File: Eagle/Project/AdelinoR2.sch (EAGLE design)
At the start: 79 parts, among them J1 DC-044-A, J2 YELLOW-8P-2.54, J3 YELLOW-6P-2.54, J4 YELLOW-8P-2.54, J5 YELLOW-8P-2.54, J6 4P-2.0, J7 YELLOW-2X3P-2.54, J8 4P-2.0, Q1 NCE3407A, Q2 CJ2305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

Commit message: Routing wip.
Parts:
- removed D1, D2: 1K 1/10W, Seeed-Fuse:SMD-ESD-CG0603MLC-05E
- added ESD1: PRTR5V0U2X, Seeed-OPL-2017-01-Diode-james:SMD-DIODE-TVS-5.5V
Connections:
- net GND: no longer D1.1, D2.1
- net N$1: now also ESD1.IO2; no longer D1.2
- net N$2: now also ESD1.IO1; no longer D2.2
- net N$9: now also ESD1.VCC
- net UGND: now also ESD1.GND
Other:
- moved on the sheet: F1, L1, R2, R3, USB1

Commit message: Add ATECC608 crypto chip; routing wip.
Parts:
- added U6: ATECC608-SOIC8, Adelino-Misc:ATECC608(SOIC8)
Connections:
- removed net PIN_D2: J5.3, J6.2, U3.GPIO4, U4.PD1(SDA/INT1), U5.PD1(SDA/INT1)
- removed net PIN_D3: J5.4, J6.1, U3.GPIO5, U4.PD0(OC0B/SCL/INT0), U5.PD0(OC0B/SCL/INT0)
- removed net _ESP: D8.+, R28.2
- new net N$4: D8.-, R28.1
- new net PIN_D2_SDA: J5.3, J6.2, U3.GPIO4, U4.PD1(SDA/INT1), U5.PD1(SDA/INT1), U6.SDA
- new net PIN_D3_SCL: J5.4, J6.1, U3.GPIO5, U4.PD0(OC0B/SCL/INT0), U5.PD0(OC0B/SCL/INT0), U6.SCL
- net +3V3: now also D8.+; no longer R28.1
- net +5V: now also U6.VCC
- net GND: now also U6.GND
- net GPIO2_LED: now also R28.2; no longer D8.-
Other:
- note added: "Security"
- moved on the sheet: D4, D5, D6, D7, D8, R13, R14, R15, R16, R17, R18, R19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

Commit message: Routing wip.
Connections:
- net +3V3: now also R28.1; no longer D8.+
- net GPIO2_LED: now also D8.-; no longer R28.2
- net N$4: now also D8.+, R28.2; no longer D8.-, R28.1
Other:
- note added: "ICSP"
- moved on the sheet: D8, R28
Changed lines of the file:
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@@
 <setting verticaltext="up"/>
 </settings>
-<grid distance="0.05" unitdist="inch" unit="inch" style="lines" multiple="1" display="no" altdistance="0.01" altunitdist="inch" altunit="inch"/>
+<grid distance="0.1" unitdist="inch" unit="inch" style="lines" multiple="1" display="no" altdistance="0.01" altunitdist="inch" altunit="inch"/>
 <layers>
 <layer number="1" name="Top" color="4" fill="1" visible="no" active="no"/>
@@
 <text x="-66.04" y="-85.09" size="2.54" layer="97">Grove Serial</text>
 <text x="13.97" y="-125.73" size="6.4516" layer="97">Security</text>
+<text x="-79.248" y="-130.556" size="2.54" layer="97">ICSP</text>
 </plain>
 <instances>
@@
 <attribute name="VALUE" x="71.628" y="-54.356" size="1.27" layer="96" ratio="10"/>
 </instance>
-<instance part="D8" gate="G$1" x="191.77" y="-101.6" smashed="yes">
-<attribute name="NAME" x="189.992" y="-99.822" size="1.27" layer="95" ratio="10" rot="R180"/>
-<attribute name="VALUE" x="193.548" y="-103.124" size="1.016" layer="96" ratio="10"/>
-<attribute name="LABEL" x="193.548" y="-101.092" size="1.4224" layer="96"/>
+<instance part="D8" gate="G$1" x="201.93" y="-101.6" smashed="yes">
+<attribute name="NAME" x="200.152" y="-99.822" size="1.27" layer="95" ratio="10" rot="R180"/>
+<attribute name="VALUE" x="203.708" y="-103.124" size="1.016" layer="96" ratio="10"/>
+<attribute name="LABEL" x="203.708" y="-101.092" size="1.4224" layer="96"/>
 </instance>
 <instance part="+3V34" gate="G$1" x="182.88" y="-93.726" smashed="yes">
@@
 <attribute name="VALUE" x="71.628" y="-92.456" size="1.27" layer="96" ratio="10"/>
 </instance>
-<instance part="R28" gate="G$1" x="201.93" y="-101.6" smashed="yes">
-<attribute name="NAME" x="203.708" y="-101.092" size="1.27" layer="95" ratio="10"/>
-<attribute name="VALUE" x="203.708" y="-103.378" size="1.27" layer="96" ratio="10"/>
+<instance part="R28" gate="G$1" x="191.77" y="-101.6" smashed="yes">
+<attribute name="NAME" x="193.548" y="-101.092" size="1.27" layer="95" ratio="10"/>
+<attribute name="VALUE" x="193.548" y="-103.378" size="1.27" layer="96" ratio="10"/>
 </instance>
 <instance part="R29" gate="G$1" x="191.77" y="-109.22" smashed="yes">
@@
 <wire x1="187.96" y1="-109.22" x2="182.88" y2="-109.22" width="0.1524" layer="91"/>
 <wire x1="182.88" y1="-109.22" x2="182.88" y2="-101.6" width="0.1524" layer="91"/>
-<pinref part="D8" gate="G$1" pin="+"/>
+<pinref part="R28" gate="G$1" pin="1"/>
 <wire x1="182.88" y1="-101.6" x2="182.88" y2="-96.266" width="0.1524" layer="91"/>
 <wire x1="187.96" y1="-101.6" x2="182.88" y2="-101.6" width="0.1524" layer="91"/>
@@
 <junction x="212.09" y="-109.22"/>
 <label x="226.06" y="-109.22" size="1.4224" layer="95" rot="R180"/>
-<pinref part="R28" gate="G$1" pin="2"/>
+<pinref part="D8" gate="G$1" pin="-"/>
 <wire x1="205.74" y1="-101.6" x2="212.09" y2="-101.6" width="0.1524" layer="91"/>
 </segment>
@@
 <net name="N$4" class="0">
 <segment>
-<pinref part="R28" gate="G$1" pin="1"/>
-<pinref part="D8" gate="G$1" pin="-"/>
+<pinref part="D8" gate="G$1" pin="+"/>
+<pinref part="R28" gate="G$1" pin="2"/>
 <wire x1="198.12" y1="-101.6" x2="195.58" y2="-101.6" width="0.1524" layer="91"/>
 </segment>

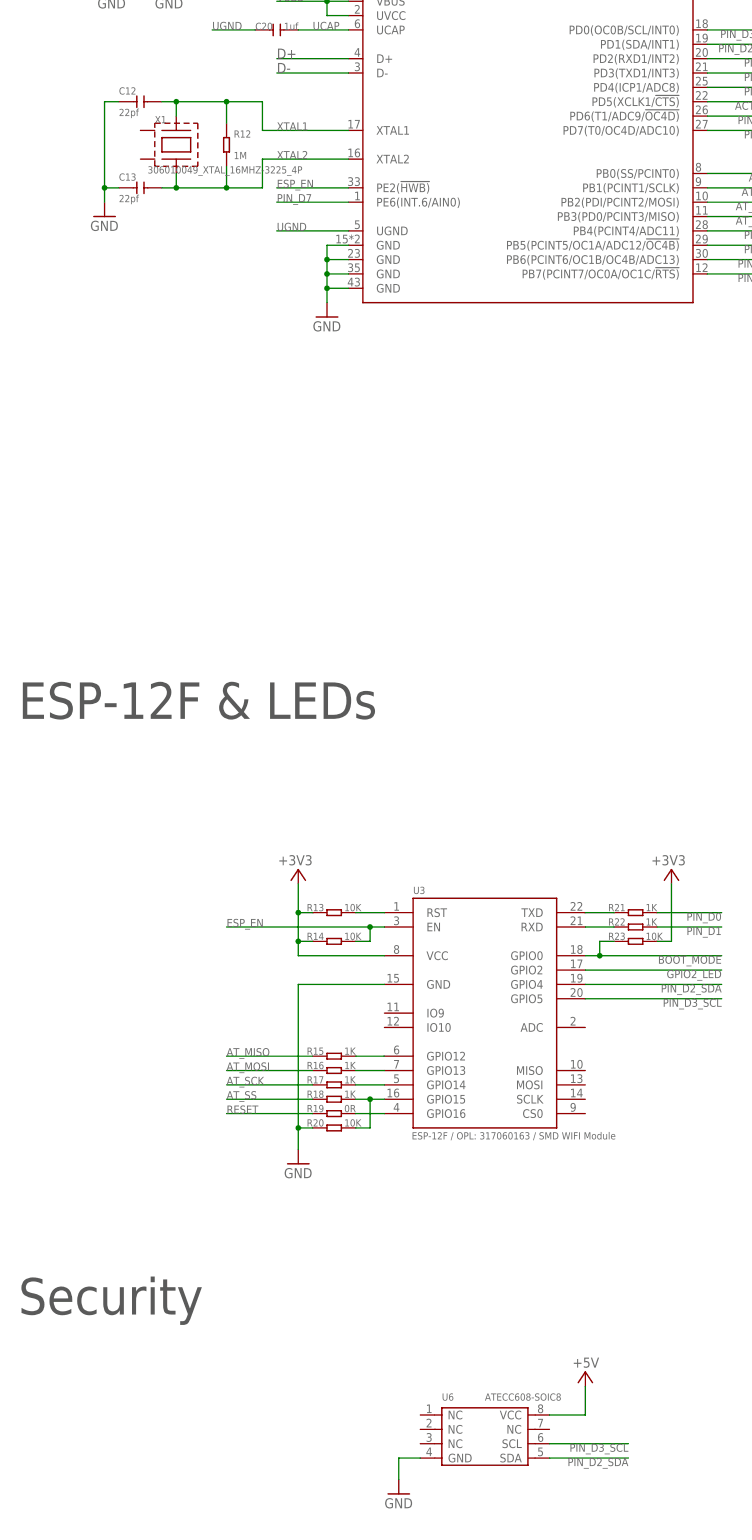
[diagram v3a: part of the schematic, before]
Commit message: Add decoupling cap for ECC608.
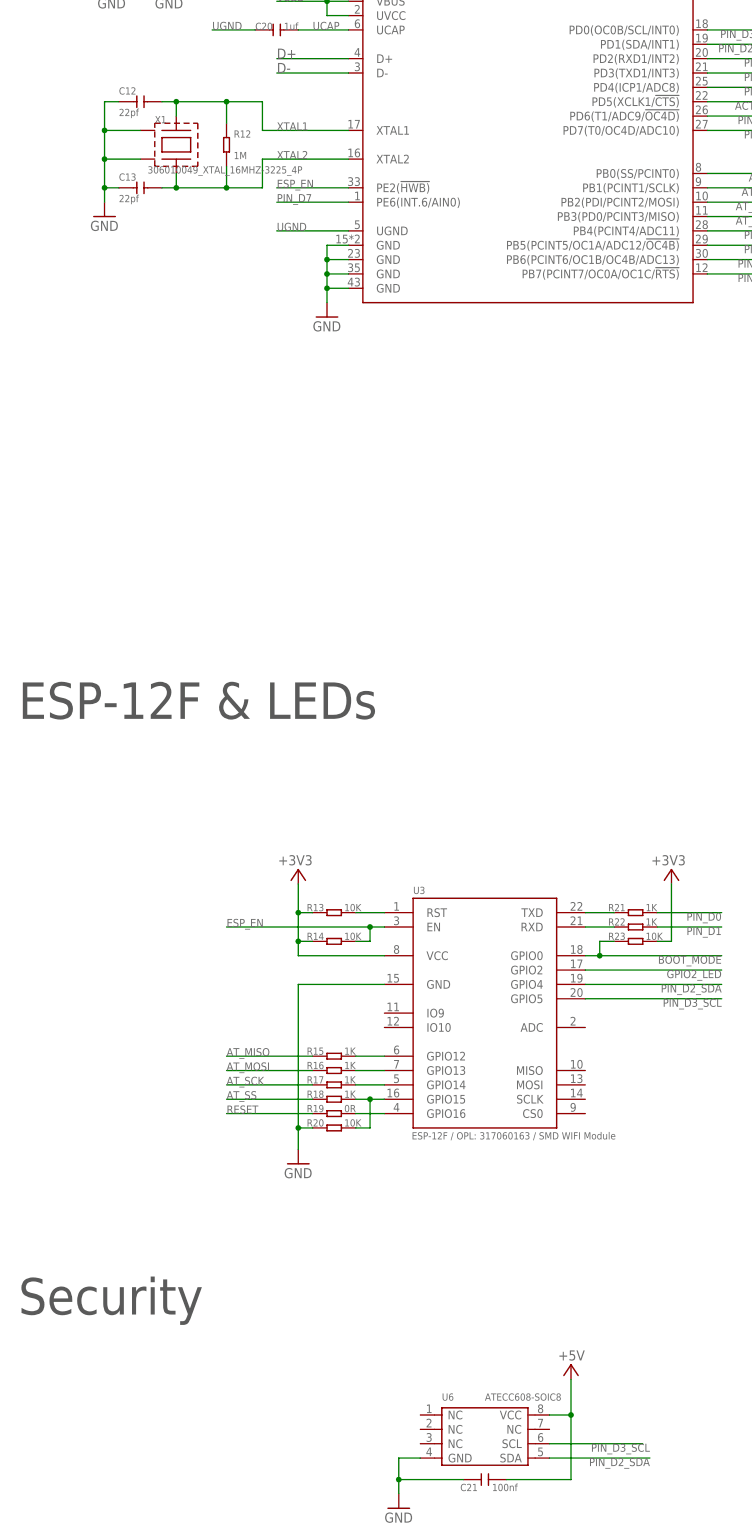
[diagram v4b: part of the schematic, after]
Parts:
- added C21: 100nf, Seeed-Capacitor:CERAMIC-100NF-25V-10%-X7R(0402)
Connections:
- net +5V: now also C21.1
- net GND: now also C21.2, X1.GND1, X1.GND2
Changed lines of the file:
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@@
 <setting verticaltext="up"/>
 </settings>
-<grid distance="0.1" unitdist="inch" unit="inch" style="lines" multiple="1" display="no" altdistance="0.01" altunitdist="inch" altunit="inch"/>
+<grid distance="0.05" unitdist="inch" unit="inch" style="lines" multiple="1" display="yes" altdistance="0.01" altunitdist="inch" altunit="inch"/>
 <layers>
 <layer number="1" name="Top" color="4" fill="1" visible="no" active="no"/>
@@
 <part name="GND14" library="supply1" library_urn="urn:adsk.eagle:library:371" deviceset="GND" device=""/>
 <part name="P+8" library="supply1" library_urn="urn:adsk.eagle:library:371" deviceset="+5V" device=""/>
+<part name="C21" library="Seeed-Capacitor" deviceset="CERAMIC-100NF-25V-10%-X7R(0402)" device="" value="100nf"/>
 </parts>
 <sheets>
@@
 <attribute name="VALUE" x="96.52" y="-140.97" size="1.27" layer="96" ratio="10"/>
 </instance>
-<instance part="GND14" gate="1" x="81.28" y="-157.48" smashed="yes">
-<attribute name="VALUE" x="78.74" y="-160.02" size="1.778" layer="96"/>
-</instance>
-<instance part="P+8" gate="1" x="114.3" y="-135.89" smashed="yes">
-<attribute name="VALUE" x="112.014" y="-135.128" size="1.778" layer="96"/>
+<instance part="GND14" gate="1" x="81.28" y="-160.02" smashed="yes">
+<attribute name="VALUE" x="78.74" y="-162.56" size="1.778" layer="96"/>
+</instance>
+<instance part="P+8" gate="1" x="111.76" y="-134.62" smashed="yes">
+<attribute name="VALUE" x="109.474" y="-133.858" size="1.778" layer="96"/>
+</instance>
+<instance part="C21" gate="G$1" x="96.52" y="-154.94" smashed="yes" rot="R180">
+<attribute name="NAME" x="95.25" y="-155.702" size="1.27" layer="95" ratio="10" rot="R180"/>
+<attribute name="VALUE" x="97.79" y="-156.972" size="1.27" layer="96" ratio="10"/>
 </instance>
 </instances>
@@
 <wire x1="31.75" y1="88.9" x2="29.21" y2="88.9" width="0.1524" layer="91"/>
 <junction x="29.21" y="73.66"/>
-<wire x1="29.21" y1="88.9" x2="29.21" y2="73.66" width="0.1524" layer="91"/>
+<wire x1="29.21" y1="88.9" x2="29.21" y2="83.82" width="0.1524" layer="91"/>
 <pinref part="C12" gate="G$1" pin="1"/>
 <pinref part="C13" gate="G$1" pin="1"/>
+<pinref part="X1" gate="G$1" pin="GND1"/>
+<wire x1="29.21" y1="83.82" x2="29.21" y2="78.74" width="0.1524" layer="91"/>
+<wire x1="29.21" y1="78.74" x2="29.21" y2="73.66" width="0.1524" layer="91"/>
+<wire x1="35.56" y1="83.82" x2="29.21" y2="83.82" width="0.1524" layer="91"/>
+<junction x="29.21" y="83.82"/>
+<pinref part="X1" gate="G$1" pin="GND2"/>
+<wire x1="35.56" y1="78.74" x2="29.21" y2="78.74" width="0.1524" layer="91"/>
+<junction x="29.21" y="78.74"/>
 </segment>
 <segment>
@@
 <pinref part="GND14" gate="1" pin="GND"/>
 <pinref part="U6" gate="G$1" pin="GND"/>
+<wire x1="81.28" y1="-157.48" x2="81.28" y2="-154.94" width="0.1524" layer="91"/>
 <wire x1="81.28" y1="-154.94" x2="81.28" y2="-151.13" width="0.1524" layer="91"/>
 <wire x1="81.28" y1="-151.13" x2="85.09" y2="-151.13" width="0.1524" layer="91"/>
+<pinref part="C21" gate="G$1" pin="2"/>
+<wire x1="81.28" y1="-154.94" x2="92.71" y2="-154.94" width="0.1524" layer="91"/>
+<junction x="81.28" y="-154.94"/>
 </segment>
 </net>
@@
 <pinref part="U6" gate="G$1" pin="VCC"/>
 <pinref part="P+8" gate="1" pin="+5V"/>
-<wire x1="107.95" y1="-143.51" x2="114.3" y2="-143.51" width="0.1524" layer="91"/>
-<wire x1="114.3" y1="-143.51" x2="114.3" y2="-138.43" width="0.1524" layer="91"/>
+<wire x1="107.95" y1="-143.51" x2="111.76" y2="-143.51" width="0.1524" layer="91"/>
+<wire x1="111.76" y1="-143.51" x2="111.76" y2="-137.16" width="0.1524" layer="91"/>
+<pinref part="C21" gate="G$1" pin="1"/>
+<wire x1="100.33" y1="-154.94" x2="111.76" y2="-154.94" width="0.1524" layer="91"/>
+<wire x1="111.76" y1="-154.94" x2="111.76" y2="-143.51" width="0.1524" layer="91"/>
+<junction x="111.76" y="-143.51"/>
 </segment>
 </net>
@@
 <segment>
 <pinref part="U6" gate="G$1" pin="SCL"/>
-<wire x1="107.95" y1="-148.59" x2="121.92" y2="-148.59" width="0.1524" layer="91"/>
-<label x="121.92" y="-148.59" size="1.4224" layer="95" rot="R180"/>
+<wire x1="107.95" y1="-148.59" x2="124.46" y2="-148.59" width="0.1524" layer="91"/>
+<label x="125.73" y="-148.59" size="1.4224" layer="95" rot="R180"/>
 </segment>
 </net>
@@
 <segment>
 <pinref part="U6" gate="G$1" pin="SDA"/>
-<wire x1="107.95" y1="-151.13" x2="121.92" y2="-151.13" width="0.1524" layer="91"/>
-<label x="121.92" y="-151.13" size="1.4224" layer="95" rot="R180"/>
-</segment>
-</net>
+<wire x1="107.95" y1="-151.13" x2="125.73" y2="-151.13" width="0.1524" layer="91"/>
+<label x="125.73" y="-151.13" size="1.4224" layer="95" rot="R180"/>
+</segment>
+</net>

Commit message: Add 15V TVS from Shenzhen OPL.
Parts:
- removed TVS1: (no value), Seeed-OPL-2017-01-Diode-james:SMD-DIODE-TVS-7VWM-22.7VC-SOD-523
- added D1: SMBJ15CA-13-F, Adelino-Misc:SMBJ15CA-13-F
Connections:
- net GND: now also D1.+; no longer TVS1.+
- net VIN: now also D1.-; no longer TVS1.-
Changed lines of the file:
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@@
 <?xml version="1.0" encoding="utf-8"?>
 <!DOCTYPE eagle SYSTEM "eagle.dtd">
-<eagle version="9.2.2">
+<eagle version="9.2.1">
 <drawing>
 <settings>
@@
 <setting verticaltext="up"/>
 </settings>
-<grid distance="0.05" unitdist="inch" unit="inch" style="lines" multiple="1" display="yes" altdistance="0.01" altunitdist="inch" altunit="inch"/>
+<grid distance="0.05" unitdist="inch" unit="inch" style="lines" multiple="1" display="no" altdistance="0.01" altunitdist="inch" altunit="inch"/>
 <layers>
 <layer number="1" name="Top" color="4" fill="1" visible="no" active="no"/>
@@
 <part name="GND12" library="supply1" library_urn="urn:adsk.eagle:library:371" deviceset="GND" device=""/>
 <part name="P+6" library="supply1" library_urn="urn:adsk.eagle:library:371" deviceset="+5V" device=""/>
-<part name="TVS1" library="Seeed-OPL-2017-01-Diode-james" deviceset="SMD-DIODE-TVS-7VWM-22.7VC-SOD-523" device=""/>
 <part name="R26" library="Seeed-Resistor" deviceset="SMD-RES-1K-5%-1/16W(0402)" device="" value="1K"/>
 <part name="R24" library="Seeed-Resistor" deviceset="SMD-RES-1K-5%-1/16W(0402)" device="" value="1K"/>
@@
 <part name="P+8" library="supply1" library_urn="urn:adsk.eagle:library:371" deviceset="+5V" device=""/>
 <part name="C21" library="Seeed-Capacitor" deviceset="CERAMIC-100NF-25V-10%-X7R(0402)" device="" value="100nf"/>
+<part name="D1" library="Adelino-Misc" deviceset="SMBJ15CA-13-F" device=""/>
 </parts>
 <sheets>
@@
 <attribute name="VALUE" x="166.37" y="140.97" size="1.778" layer="96" rot="R180"/>
 </instance>
-<instance part="TVS1" gate="G$1" x="-199.39" y="133.35" smashed="yes" rot="R90">
-<attribute name="NAME" x="-204.47" y="135.89" size="1.27" layer="95" ratio="10"/>
-<attribute name="VALUE" x="-195.58" y="129.54" size="1.27" layer="96" ratio="10" rot="R90"/>
-</instance>
 <instance part="R26" gate="G$1" x="191.77" y="-73.66" smashed="yes">
 <attribute name="NAME" x="189.992" y="-71.882" size="1.27" layer="95" ratio="10" rot="R180"/>
@@
 <attribute name="NAME" x="95.25" y="-155.702" size="1.27" layer="95" ratio="10" rot="R180"/>
 <attribute name="VALUE" x="97.79" y="-156.972" size="1.27" layer="96" ratio="10"/>
+</instance>
+<instance part="D1" gate="G$1" x="-199.39" y="132.08" smashed="yes">
+<attribute name="NAME" x="-200.152" y="135.636" size="1.27" layer="95" ratio="10" rot="R180"/>
+<attribute name="VALUE" x="-200.152" y="129.794" size="1.27" layer="96" ratio="10" rot="R180"/>
 </instance>
 </instances>
@@
 <wire x1="-210.82" y1="138.43" x2="-207.01" y2="138.43" width="0.1524" layer="91"/>
 <wire x1="-207.01" y1="138.43" x2="-207.01" y2="121.92" width="0.1524" layer="91"/>
+<pinref part="J1" gate="G$1" pin="CDN"/>
 <wire x1="-207.01" y1="121.92" x2="-199.39" y2="121.92" width="0.1524" layer="91"/>
-<pinref part="J1" gate="G$1" pin="CDN"/>
 <wire x1="-199.39" y1="121.92" x2="-191.77" y2="121.92" width="0.1524" layer="91"/>
 <wire x1="-146.05" y1="121.92" x2="-163.83" y2="121.92" width="0.1524" layer="91"/>
@@
 <wire x1="-163.83" y1="124.46" x2="-163.83" y2="121.92" width="0.1524" layer="91"/>
 <junction x="-163.83" y="121.92"/>
-<wire x1="-199.39" y1="129.54" x2="-199.39" y2="121.92" width="0.1524" layer="91"/>
+<pinref part="D1" gate="G$1" pin="+"/>
+<wire x1="-199.39" y1="128.016" x2="-199.39" y2="121.92" width="0.1524" layer="91"/>
 <junction x="-199.39" y="121.92"/>
-<pinref part="TVS1" gate="G$1" pin="+"/>
 </segment>
 <segment>
@@
 <label x="-210.82" y="151.13" size="1.4224" layer="95"/>
 <pinref part="Q1" gate="G$1" pin="D"/>
+<junction x="-207.01" y="143.51"/>
 <wire x1="-196.85" y1="143.51" x2="-199.39" y2="143.51" width="0.1524" layer="91"/>
-<junction x="-207.01" y="143.51"/>
+<pinref part="D1" gate="G$1" pin="-"/>
 <wire x1="-199.39" y1="143.51" x2="-207.01" y2="143.51" width="0.1524" layer="91"/>
-<wire x1="-199.39" y1="137.16" x2="-199.39" y2="143.51" width="0.1524" layer="91"/>
+<wire x1="-199.39" y1="136.144" x2="-199.39" y2="143.51" width="0.1524" layer="91"/>
 <junction x="-199.39" y="143.51"/>
-<pinref part="TVS1" gate="G$1" pin="-"/>
-</segment>
-<segment>
+</segment>
+<segment>
